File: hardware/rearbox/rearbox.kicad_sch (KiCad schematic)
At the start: 22 parts, among them J1 STDC14, J2 ST-LINK, SW1 Reset, U1 LM4040C33FTA, U2 STM32G473RCTx, Y1 48MHz

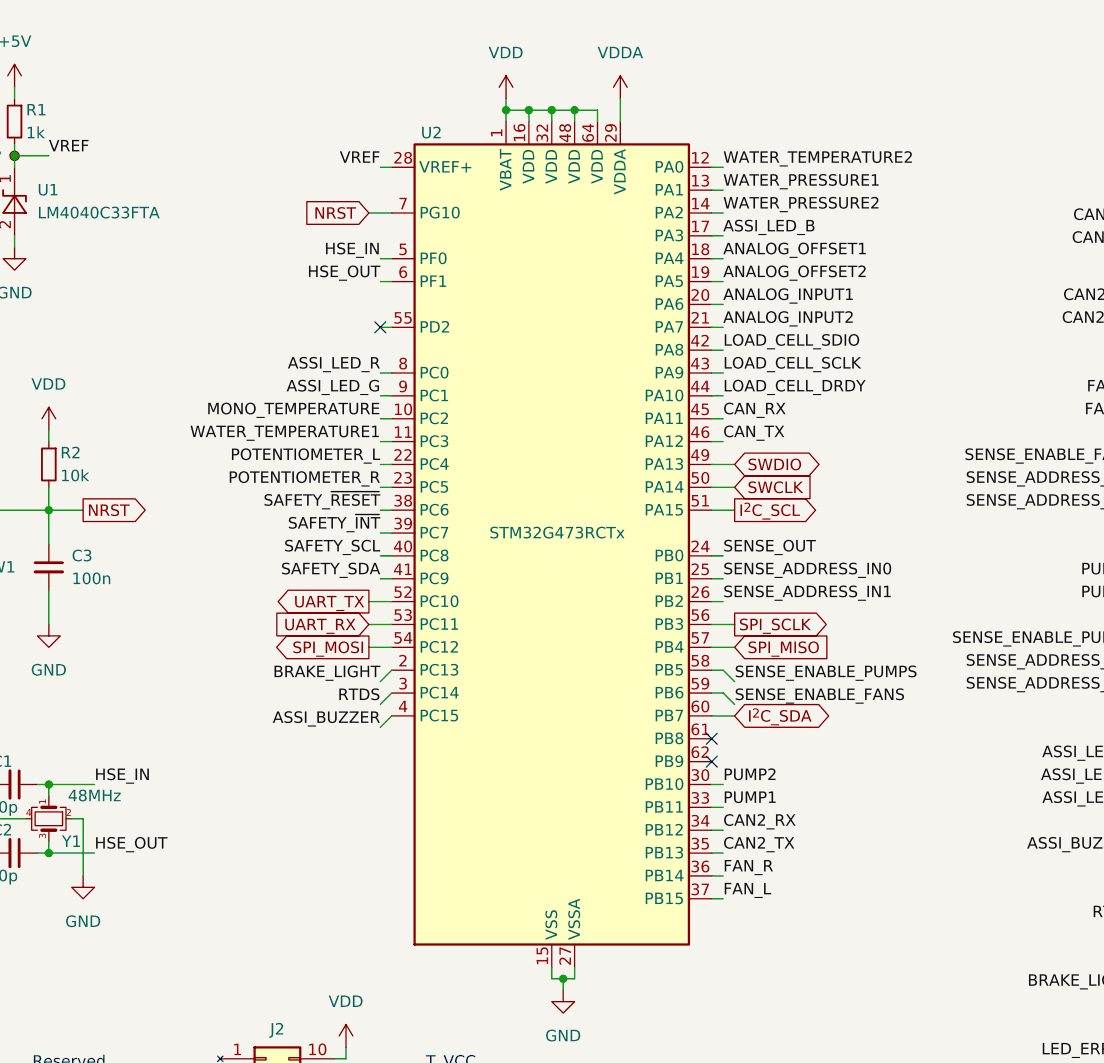
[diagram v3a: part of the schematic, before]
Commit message: Route PCB tracks
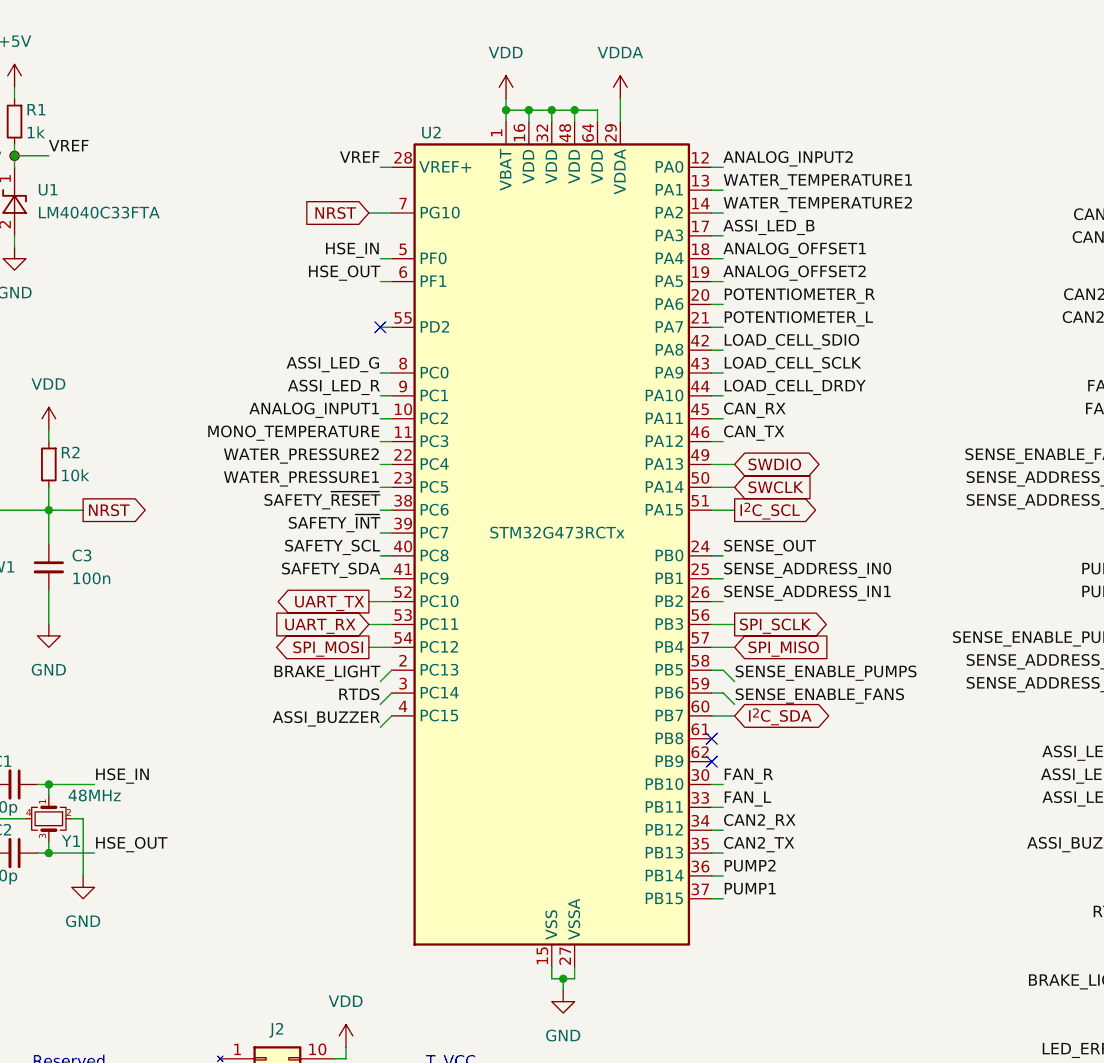
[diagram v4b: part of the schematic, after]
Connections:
- net ANALOG_INPUT1: now also U2.10 (PC2); no longer U2.20 (PA6)
- net ANALOG_INPUT2: now also U2.12 (PA0); no longer U2.21 (PA7)
- net ASSI_LED_G: now also U2.8 (PC0); no longer U2.9 (PC1)
- net ASSI_LED_R: now also U2.9 (PC1); no longer U2.8 (PC0)
- net FAN_L: now also U2.33 (PB11); no longer U2.37 (PB15)
- net FAN_R: now also U2.30 (PB10); no longer U2.36 (PB14)
- net MONO_TEMPERATURE: now also U2.11 (PC3); no longer U2.10 (PC2)
- net POTENTIOMETER_L: now also U2.21 (PA7); no longer U2.22 (PC4)
- net POTENTIOMETER_R: now also U2.20 (PA6); no longer U2.23 (PC5)
- net PUMP1: now also U2.37 (PB15); no longer U2.33 (PB11)
- net PUMP2: now also U2.36 (PB14); no longer U2.30 (PB10)
- net WATER_PRESSURE1: now also U2.23 (PC5); no longer U2.13 (PA1)
- net WATER_PRESSURE2: now also U2.22 (PC4); no longer U2.14 (PA2)
- net WATER_TEMPERATURE1: now also U2.13 (PA1); no longer U2.11 (PC3)
- net WATER_TEMPERATURE2: now also U2.14 (PA2); no longer U2.12 (PA0)
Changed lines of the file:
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@@
     (effects (font (size 1.27 1.27)) (justify left bottom))
   )
-  (label "WATER_PRESSURE1" (at 102.87 39.37 0) (fields_autoplaced)
-    (effects (font (size 1.27 1.27)) (justify left bottom))
-  )
-  (label "POTENTIOMETER_L" (at 64.77 69.85 180) (fields_autoplaced)
-    (effects (font (size 1.27 1.27)) (justify right bottom))
+  (label "WATER_PRESSURE1" (at 64.77 72.39 180) (fields_autoplaced)
+    (effects (font (size 1.27 1.27)) (justify right bottom))
+  )
+  (label "POTENTIOMETER_L" (at 102.87 54.61 0) (fields_autoplaced)
+    (effects (font (size 1.27 1.27)) (justify left bottom))
   )
   (label "SENSE_ENABLE_FANS" (at 148.59 69.85 180) (fields_autoplaced)
@@
     (effects (font (size 1.27 1.27)) (justify right bottom))
   )
-  (label "WATER_TEMPERATURE2" (at 102.87 36.83 0) (fields_autoplaced)
+  (label "WATER_TEMPERATURE2" (at 102.87 41.91 0) (fields_autoplaced)
     (effects (font (size 1.27 1.27)) (justify left bottom))
   )
@@
     (effects (font (size 1.27 1.27)) (justify left bottom))
   )
-  (label "POTENTIOMETER_R" (at 64.77 72.39 180) (fields_autoplaced)
-    (effects (font (size 1.27 1.27)) (justify right bottom))
+  (label "POTENTIOMETER_R" (at 102.87 52.07 0) (fields_autoplaced)
+    (effects (font (size 1.27 1.27)) (justify left bottom))
   )
   (label "VREF" (at 64.77 36.83 180) (fields_autoplaced)
@@
     (effects (font (size 1.27 1.27)) (justify right bottom))
   )
-  (label "MONO_TEMPERATURE" (at 64.77 64.77 180) (fields_autoplaced)
+  (label "MONO_TEMPERATURE" (at 64.77 67.31 180) (fields_autoplaced)
     (effects (font (size 1.27 1.27)) (justify right bottom))
   )
@@
     (effects (font (size 1.27 1.27)) (justify left bottom))
   )
-  (label "ANALOG_INPUT2" (at 102.87 54.61 0) (fields_autoplaced)
+  (label "ANALOG_INPUT2" (at 102.87 36.83 0) (fields_autoplaced)
     (effects (font (size 1.27 1.27)) (justify left bottom))
   )
@@
     (effects (font (size 1.27 1.27)) (justify left bottom))
   )
-  (label "ANALOG_INPUT1" (at 102.87 52.07 0) (fields_autoplaced)
-    (effects (font (size 1.27 1.27)) (justify left bottom))
+  (label "ANALOG_INPUT1" (at 64.77 64.77 180) (fields_autoplaced)
+    (effects (font (size 1.27 1.27)) (justify right bottom))
   )
   (label "SENSE_ADDRESS_IN0" (at 102.87 82.55 0) (fields_autoplaced)
@@
     (effects (font (size 1.27 1.27)) (justify left bottom))
   )
-  (label "PUMP2" (at 102.87 105.41 0) (fields_autoplaced)
+  (label "PUMP2" (at 102.87 115.57 0) (fields_autoplaced)
     (effects (font (size 1.27 1.27)) (justify left bottom))
   )
@@
     (effects (font (size 1.27 1.27)) (justify right bottom))
   )
-  (label "WATER_TEMPERATURE1" (at 64.77 67.31 180) (fields_autoplaced)
-    (effects (font (size 1.27 1.27)) (justify right bottom))
+  (label "WATER_TEMPERATURE1" (at 102.87 39.37 0) (fields_autoplaced)
+    (effects (font (size 1.27 1.27)) (justify left bottom))
   )
   (label "LED_FUSE" (at 260.35 27.94 0) (fields_autoplaced)
@@
     (effects (font (size 1.27 1.27)) (justify right bottom))
   )
-  (label "PUMP1" (at 102.87 107.95 0) (fields_autoplaced)
-    (effects (font (size 1.27 1.27)) (justify left bottom))
-  )
-  (label "ASSI_LED_R" (at 64.77 59.69 180) (fields_autoplaced)
+  (label "PUMP1" (at 102.87 118.11 0) (fields_autoplaced)
+    (effects (font (size 1.27 1.27)) (justify left bottom))
+  )
+  (label "ASSI_LED_R" (at 64.77 62.23 180) (fields_autoplaced)
     (effects (font (size 1.27 1.27)) (justify right bottom))
   )
@@
     (effects (font (size 1.27 1.27)) (justify left bottom))
   )
-  (label "WATER_PRESSURE2" (at 102.87 41.91 0) (fields_autoplaced)
-    (effects (font (size 1.27 1.27)) (justify left bottom))
+  (label "WATER_PRESSURE2" (at 64.77 69.85 180) (fields_autoplaced)
+    (effects (font (size 1.27 1.27)) (justify right bottom))
   )
   (label "SAFETY_SDA" (at 227.33 22.86 180) (fields_autoplaced)
@@
     (effects (font (size 1.27 1.27)) (justify left bottom))
   )
-  (label "FAN_R" (at 102.87 115.57 0) (fields_autoplaced)
+  (label "FAN_R" (at 102.87 105.41 0) (fields_autoplaced)
     (effects (font (size 1.27 1.27)) (justify left bottom))
   )
@@
     (effects (font (size 1.27 1.27)) (justify left bottom))
   )
-  (label "ASSI_LED_G" (at 64.77 62.23 180) (fields_autoplaced)
+  (label "ASSI_LED_G" (at 64.77 59.69 180) (fields_autoplaced)
     (effects (font (size 1.27 1.27)) (justify right bottom))
   )
@@
     (effects (font (size 1.27 1.27)) (justify right bottom))
   )
-  (label "FAN_L" (at 102.87 118.11 0) (fields_autoplaced)
-    (effects (font (size 1.27 1.27)) (justify left bottom))
-  )
+  (label "FAN_L" (at 102.87 107.95 0) (fields_autoplaced)
+    (effects (font (size 1.27 1.27)) (justify left bottom))
+  )
